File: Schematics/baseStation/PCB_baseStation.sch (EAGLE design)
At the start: 41 parts, among them U1 ATMEGA328P, U2 MCP1824ST-3302E/DB, Y2 16MHz

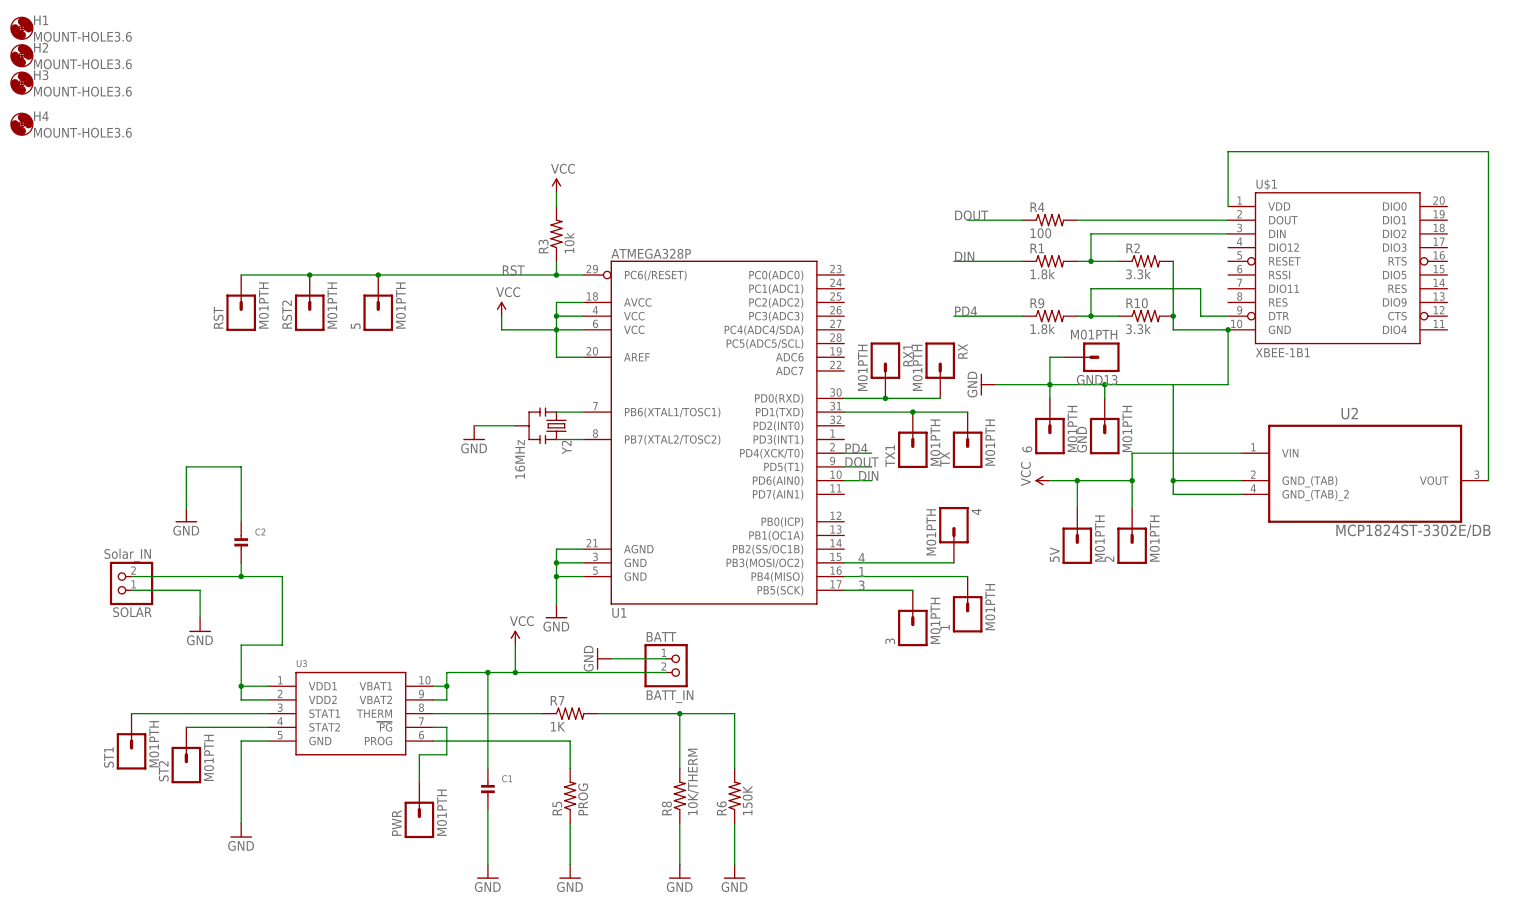
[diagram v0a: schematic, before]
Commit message: Base Station PCB Improvements
Base_SP 1.3
fixed SIM900 pins that go to Arduino
changed xbee pin that goes to Arduino
created table of base Arduino pins and where they go to
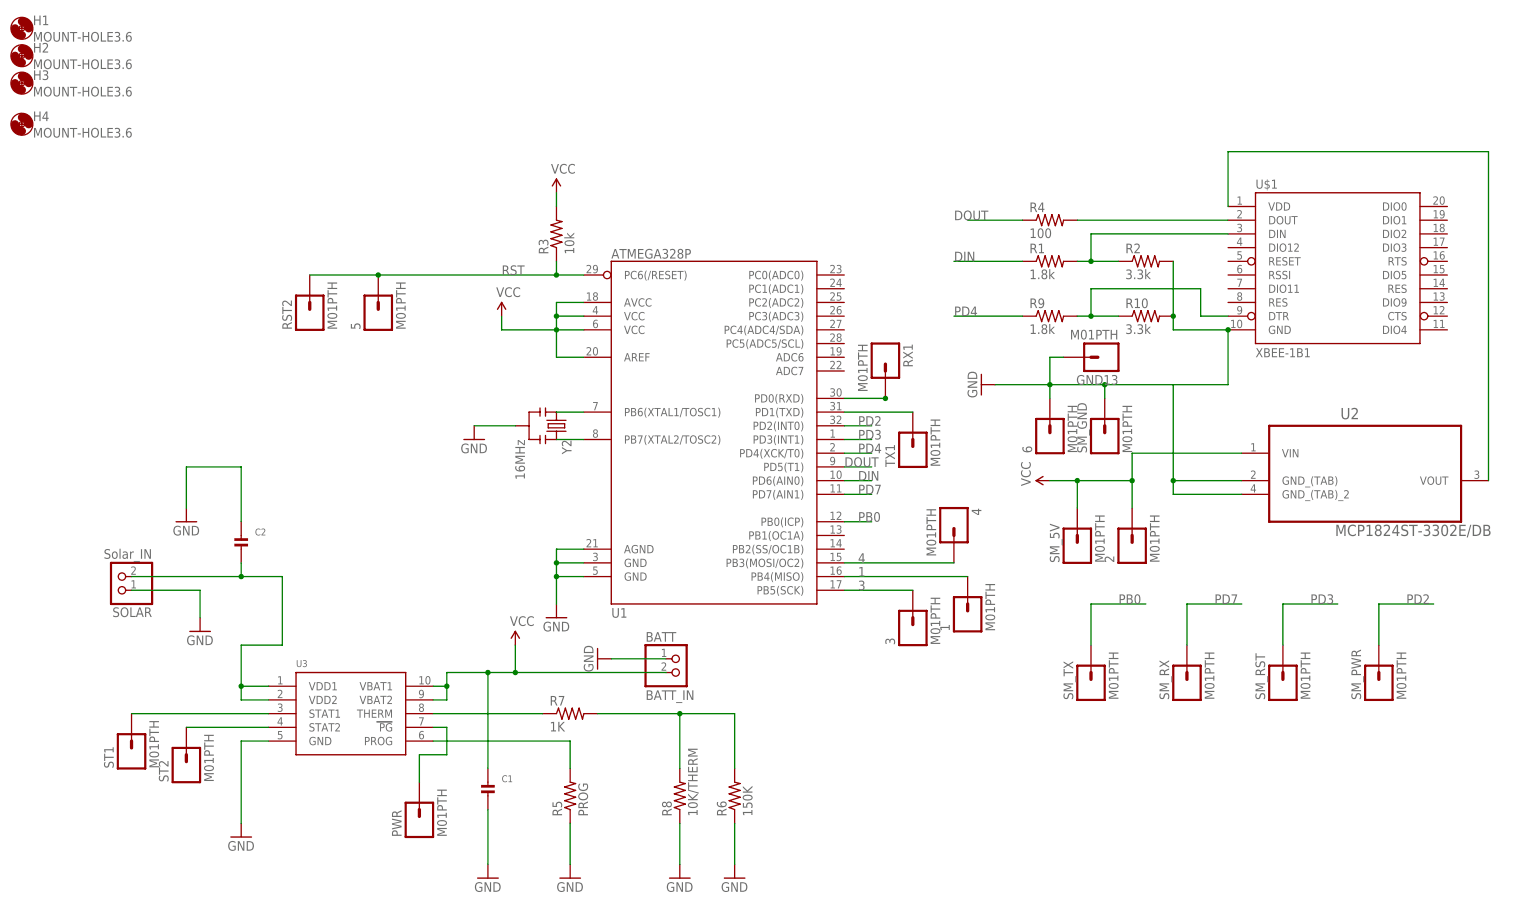
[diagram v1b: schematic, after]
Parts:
- removed RST, RX, TX: M01PTH, SparkFun-Connectors:M01PTH
- added SM_PWR, SM_RST, SM_RX, SM_TX: M01PTH, SparkFun-Connectors:M01PTH
- renumbered 5V to SM_5V, GND to SM_GND
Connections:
- new net PB0: SM_TX.1, U1.PB0(ICP)
- new net PD2: SM_PWR.1, U1.PD2(INT0)
- new net PD3: SM_RST.1, U1.PD3(INT1)
- new net PD7: SM_RX.1, U1.PD7(AIN1)
- net N$19: no longer TX.1
- net N$20: no longer RX.1
- net RST: no longer RST.1
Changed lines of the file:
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@@
 <part name="C2" library="microbuilder" deviceset="CAP_CERAMIC" device="0805"/>
 <part name="GND11" library="SparkFun-Aesthetics" deviceset="GND" device=""/>
-<part name="5V" library="SparkFun-Connectors" deviceset="M01" device="PTH"/>
-<part name="GND" library="SparkFun-Connectors" deviceset="M01" device="PTH"/>
-<part name="RST" library="SparkFun-Connectors" deviceset="M01" device="PTH"/>
+<part name="SM_5V" library="SparkFun-Connectors" deviceset="M01" device="PTH"/>
+<part name="SM_GND" library="SparkFun-Connectors" deviceset="M01" device="PTH"/>
+<part name="SM_RST" library="SparkFun-Connectors" deviceset="M01" device="PTH"/>
 <part name="3" library="SparkFun-Connectors" deviceset="M01" device="PTH"/>
 <part name="1" library="SparkFun-Connectors" deviceset="M01" device="PTH"/>
 <part name="4" library="SparkFun-Connectors" deviceset="M01" device="PTH"/>
-<part name="TX" library="SparkFun-Connectors" deviceset="M01" device="PTH"/>
-<part name="RX" library="SparkFun-Connectors" deviceset="M01" device="PTH"/>
+<part name="SM_TX" library="SparkFun-Connectors" deviceset="M01" device="PTH"/>
+<part name="SM_RX" library="SparkFun-Connectors" deviceset="M01" device="PTH"/>
 <part name="2" library="SparkFun-Connectors" deviceset="M01" device="PTH"/>
 <part name="6" library="SparkFun-Connectors" deviceset="M01" device="PTH"/>
@@
 <part name="R9" library="SparkFun-Resistors" deviceset="1.8KOHM1/10W1%(0603)" device="" value="1.8k"/>
 <part name="R10" library="SparkFun-Resistors" deviceset="3.3KOHM1/10W1%(0603)" device="" value="3.3k"/>
+<part name="SM_PWR" library="SparkFun-Connectors" deviceset="M01" device="PTH"/>
 </parts>
 <sheets>
@@
 <instance part="C2" gate="G$1" x="-81.28" y="22.86"/>
 <instance part="GND11" gate="1" x="-91.44" y="27.94"/>
-<instance part="5V" gate="G$1" x="73.66" y="22.86" rot="R90"/>
-<instance part="GND" gate="G$1" x="78.74" y="43.18" rot="R90"/>
-<instance part="RST" gate="G$1" x="-81.28" y="66.04" rot="R90"/>
+<instance part="SM_5V" gate="G$1" x="73.66" y="22.86" rot="R90"/>
+<instance part="SM_GND" gate="G$1" x="78.74" y="43.18" rot="R90"/>
+<instance part="SM_RST" gate="G$1" x="111.76" y="-2.54" rot="R90"/>
 <instance part="3" gate="G$1" x="43.18" y="7.62" rot="R90"/>
 <instance part="1" gate="G$1" x="53.34" y="10.16" rot="R90"/>
 <instance part="4" gate="G$1" x="50.8" y="27.94" rot="R270"/>
-<instance part="TX" gate="G$1" x="53.34" y="40.64" rot="R90"/>
-<instance part="RX" gate="G$1" x="48.26" y="58.42" rot="R270"/>
+<instance part="SM_TX" gate="G$1" x="76.2" y="-2.54" rot="R90"/>
+<instance part="SM_RX" gate="G$1" x="93.98" y="-2.54" rot="R90"/>
 <instance part="2" gate="G$1" x="83.82" y="22.86" rot="R90"/>
 <instance part="6" gate="G$1" x="68.58" y="43.18" rot="R90"/>
@@
 <instance part="R9" gate="G$1" x="68.58" y="66.04"/>
 <instance part="R10" gate="G$1" x="86.36" y="66.04"/>
+<instance part="SM_PWR" gate="G$1" x="129.54" y="-2.54" rot="R90"/>
 </instances>
 <busses>
@@
 <junction x="-22.86" y="73.66"/>
 <label x="-33.02" y="73.66" size="1.778" layer="95"/>
-<pinref part="RST" gate="G$1" pin="1"/>
 <wire x1="-22.86" y1="73.66" x2="-55.88" y2="73.66" width="0.1524" layer="91"/>
 <pinref part="5" gate="G$1" pin="1"/>
@@
 <junction x="-55.88" y="73.66"/>
 <pinref part="RST2" gate="G$1" pin="1"/>
-<wire x1="-68.58" y1="73.66" x2="-81.28" y2="73.66" width="0.1524" layer="91"/>
-<junction x="-68.58" y="73.66"/>
 </segment>
 </net>
@@
 <wire x1="101.6" y1="53.34" x2="78.74" y2="53.34" width="0.1524" layer="91"/>
 <pinref part="GND1" gate="1" pin="GND"/>
-<pinref part="GND" gate="G$1" pin="1"/>
+<pinref part="SM_GND" gate="G$1" pin="1"/>
 <wire x1="78.74" y1="53.34" x2="68.58" y2="53.34" width="0.1524" layer="91"/>
 <wire x1="68.58" y1="53.34" x2="58.42" y2="53.34" width="0.1524" layer="91"/>
@@
 <wire x1="83.82" y1="35.56" x2="73.66" y2="35.56" width="0.1524" layer="91"/>
 <pinref part="SUPPLY3" gate="G$1" pin="VCC"/>
-<pinref part="5V" gate="G$1" pin="1"/>
+<pinref part="SM_5V" gate="G$1" pin="1"/>
 <wire x1="73.66" y1="35.56" x2="68.58" y2="35.56" width="0.1524" layer="91"/>
 <wire x1="73.66" y1="30.48" x2="73.66" y2="35.56" width="0.1524" layer="91"/>
@@
 <net name="N$19" class="0">
 <segment>
-<pinref part="TX" gate="G$1" pin="1"/>
 <pinref part="U1" gate="G$1" pin="PD1(TXD)"/>
-<wire x1="53.34" y1="48.26" x2="43.18" y2="48.26" width="0.1524" layer="91"/>
 <pinref part="TX1" gate="G$1" pin="1"/>
 <wire x1="43.18" y1="48.26" x2="30.48" y2="48.26" width="0.1524" layer="91"/>
-<junction x="43.18" y="48.26"/>
 </segment>
 </net>
 <net name="N$20" class="0">
 <segment>
-<pinref part="RX" gate="G$1" pin="1"/>
 <pinref part="U1" gate="G$1" pin="PD0(RXD)"/>
-<wire x1="48.26" y1="50.8" x2="38.1" y2="50.8" width="0.1524" layer="91"/>
 <pinref part="RX1" gate="G$1" pin="1"/>
 <wire x1="38.1" y1="50.8" x2="30.48" y2="50.8" width="0.1524" layer="91"/>
 <junction x="38.1" y="50.8"/>
-</segment>
-</net>
-<net name="PD4" class="0">
-<segment>
-<pinref part="U1" gate="G$1" pin="PD4(XCK/T0)"/>
-<wire x1="30.48" y1="40.64" x2="35.56" y2="40.64" width="0.1524" layer="91"/>
-<label x="30.48" y="40.64" size="1.778" layer="95"/>
-</segment>
-<segment>
-<pinref part="R9" gate="G$1" pin="1"/>
-<wire x1="63.5" y1="66.04" x2="50.8" y2="66.04" width="0.1524" layer="91"/>
-<label x="50.8" y="66.04" size="1.778" layer="95"/>
 </segment>
 </net>
@@
 </segment>
 </net>
+<net name="PD7" class="0">
+<segment>
+<pinref part="U1" gate="G$1" pin="PD7(AIN1)"/>
+<wire x1="30.48" y1="33.02" x2="35.56" y2="33.02" width="0.1524" layer="91"/>
+<label x="33.02" y="33.02" size="1.778" layer="95"/>
+</segment>
+<segment>
+<pinref part="SM_RX" gate="G$1" pin="1"/>
+<wire x1="93.98" y1="5.08" x2="93.98" y2="12.7" width="0.1524" layer="91"/>
+<wire x1="93.98" y1="12.7" x2="104.14" y2="12.7" width="0.1524" layer="91"/>
+<label x="99.06" y="12.7" size="1.778" layer="95"/>
+</segment>
+</net>
+<net name="PB0" class="0">
+<segment>
+<pinref part="U1" gate="G$1" pin="PB0(ICP)"/>
+<wire x1="30.48" y1="27.94" x2="35.56" y2="27.94" width="0.1524" layer="91"/>
+<label x="33.02" y="27.94" size="1.778" layer="95"/>
+</segment>
+<segment>
+<pinref part="SM_TX" gate="G$1" pin="1"/>
+<wire x1="76.2" y1="5.08" x2="76.2" y2="12.7" width="0.1524" layer="91"/>
+<wire x1="76.2" y1="12.7" x2="86.36" y2="12.7" width="0.1524" layer="91"/>
+<label x="81.28" y="12.7" size="1.778" layer="95"/>
+</segment>
+</net>
+<net name="PD4" class="0">
+<segment>
+<pinref part="U1" gate="G$1" pin="PD4(XCK/T0)"/>
+<wire x1="30.48" y1="40.64" x2="35.56" y2="40.64" width="0.1524" layer="91"/>
+<label x="33.02" y="40.64" size="1.778" layer="95"/>
+</segment>
+<segment>
+<pinref part="R9" gate="G$1" pin="1"/>
+<wire x1="63.5" y1="66.04" x2="50.8" y2="66.04" width="0.1524" layer="91"/>
+<label x="50.8" y="66.04" size="1.778" layer="95"/>
+</segment>
+</net>
+<net name="PD2" class="0">
+<segment>
+<pinref part="U1" gate="G$1" pin="PD2(INT0)"/>
+<wire x1="30.48" y1="45.72" x2="35.56" y2="45.72" width="0.1524" layer="91"/>
+<label x="33.02" y="45.72" size="1.778" layer="95"/>
+</segment>
+<segment>
+<pinref part="SM_PWR" gate="G$1" pin="1"/>
+<wire x1="129.54" y1="5.08" x2="129.54" y2="12.7" width="0.1524" layer="91"/>
+<wire x1="129.54" y1="12.7" x2="139.7" y2="12.7" width="0.1524" layer="91"/>
+<label x="134.62" y="12.7" size="1.778" layer="95"/>
+</segment>
+</net>
+<net name="PD3" class="0">
+<segment>
+<pinref part="U1" gate="G$1" pin="PD3(INT1)"/>
+<wire x1="30.48" y1="43.18" x2="35.56" y2="43.18" width="0.1524" layer="91"/>
+<label x="33.02" y="43.18" size="1.778" layer="95"/>
+</segment>
+<segment>
+<pinref part="SM_RST" gate="G$1" pin="1"/>
+<wire x1="111.76" y1="5.08" x2="111.76" y2="12.7" width="0.1524" layer="91"/>
+<wire x1="111.76" y1="12.7" x2="121.92" y2="12.7" width="0.1524" layer="91"/>
+<label x="116.84" y="12.7" size="1.778" layer="95"/>
+</segment>
+</net>
